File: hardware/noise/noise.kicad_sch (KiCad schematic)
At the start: 66 parts, among them J1 Conn_02x05_Odd_Even, J2 White, J3 Pink, J4 Blue, J5 Grainy, J6 HP Grainy, Q1 BC547, U1 TL074, U2 TL072

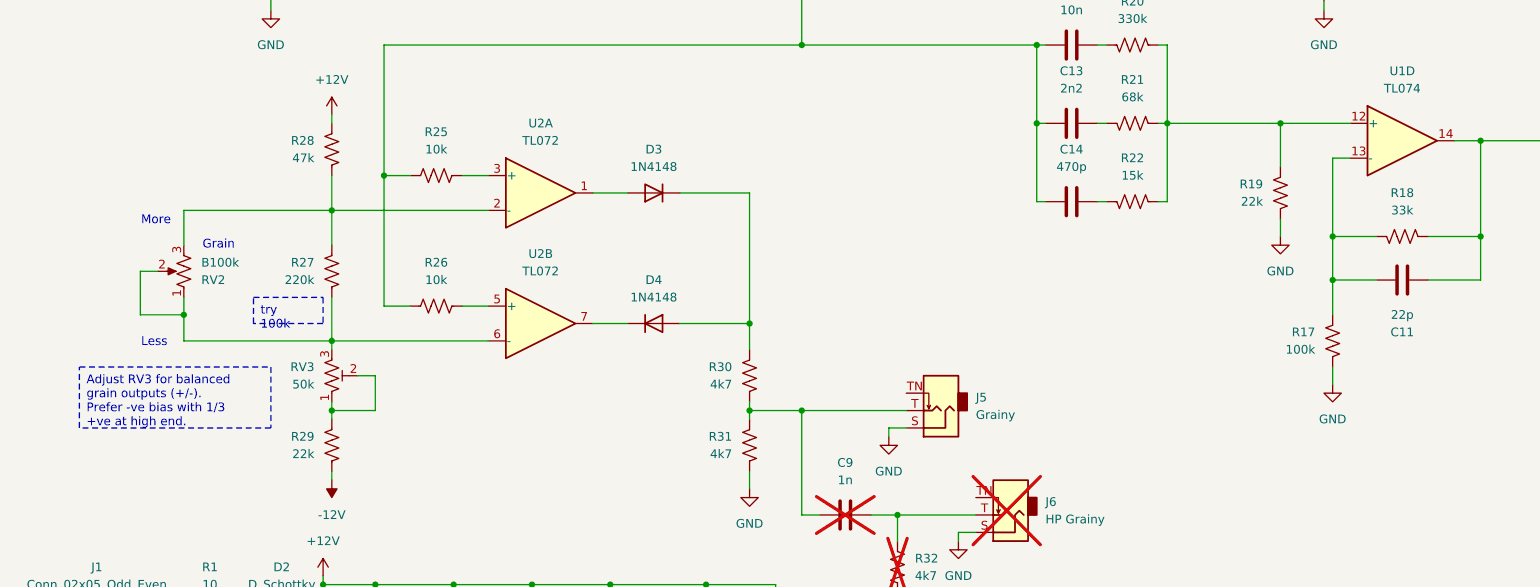
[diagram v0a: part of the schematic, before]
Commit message: finished design checks on grain output and update schematic/layout to v1.1
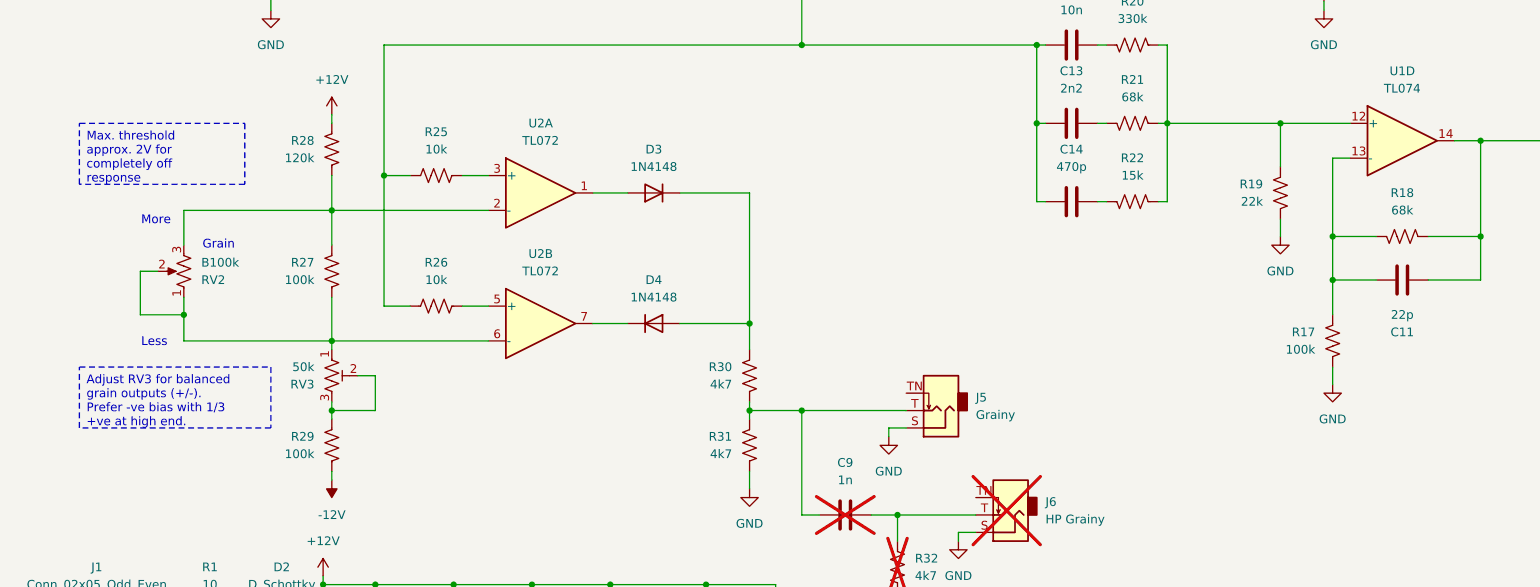
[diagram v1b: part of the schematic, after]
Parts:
- C12, C6: footprint Capacitor_THT:C_Rect_L13.0mm_W4.0mm_P10.00mm_FKS3_FKP3_MKS4 -> Capacitor_THT:C_Rect_L7.0mm_W3.5mm_P5.00mm
- C14, C8: footprint Capacitor_THT:C_Rect_L7.0mm_W3.5mm_P5.00mm -> Capacitor_THT:C_Disc_D4.7mm_W2.5mm_P5.00mm
- J2, J3, J4, J5, J6: footprint AudioJacks:Jack_3.5mm_QingPu_WQP-PJ316M_Horizontal_1 -> AudioJacks:Jack_3.5mm_QingPu_WQP-PJ323M_Horizontal
- R18: value 33k -> 68k
- R27: value 220k -> 100k
- R28: value 47k -> 120k
- R29: value 22k -> 100k
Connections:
- net at R27.2, RV2.1, RV2.2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: now also RV3.1; no longer RV3.3
- net at R29.1, RV3.2: now also RV3.3; no longer RV3.1
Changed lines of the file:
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@@
 	(title_block
 		(title "Random Noise")
-		(date "2025-02-07")
-		(rev "1.0")
+		(date "2025-03-08")
+		(rev "1.1")
 		(company "idyllm")
 		(comment 1 "CC BY-SA 4.0")
@@
 		)
 	)
-	(text_box "Adjust RV3 for balanced grain outputs (+/-).\nPrefer -ve bias with 1/3 +ve at high end."
+	(text_box "Max. threshold approx. 2V for completely off response"
 		(exclude_from_sim no)
-		(at 33.02 139.7 0)
-		(size 27.94 8.89)
+		(at 33.02 104.14 0)
+		(size 24.13 8.89)
 		(stroke
 			(width 0)
@@
 		)
 	)
-	(text_box "try 100k"
+	(text_box "Adjust RV3 for balanced grain outputs (+/-).\nPrefer -ve bias with 1/3 +ve at high end."
 		(exclude_from_sim no)
-		(at 58.42 129.54 0)
-		(size 10.16 3.81)
+		(at 33.02 139.7 0)
+		(size 27.94 8.89)
 		(stroke
 			(width 0)
@@
 			)
 		)
-		(property "Footprint" "AudioJacks:Jack_3.5mm_QingPu_WQP-PJ316M_Horizontal_1"
+		(property "Footprint" "AudioJacks:Jack_3.5mm_QingPu_WQP-PJ323M_Horizontal"
 			(at 168.91 161.29 0)
 			(effects
@@
 			)
 		)
-		(property "Value" "47k"
+		(property "Value" "120k"
 			(at 67.31 109.2199 0)
 			(effects
@@
 			)
 		)
-		(property "Value" "220k"
+		(property "Value" "100k"
 			(at 67.31 126.9999 0)
 			(effects
@@
 		(lib_id "Device:R_Potentiometer_Trim_US")
 		(at 69.85 140.97 0)
-		(mirror x)
 		(unit 1)
 		(exclude_from_sim no)
@@
 		(on_board yes)
 		(dnp no)
-		(fields_autoplaced yes)
 		(property "Reference" "RV3"
-			(at 67.31 139.6999 0)
+			(at 67.31 142.2401 0)
 			(effects
 				(font
@@
 		)
 		(property "Value" "50k"
-			(at 67.31 142.2399 0)
+			(at 67.31 139.7001 0)
 			(effects
 				(font
@@
 			)
 		)
-		(property "Footprint" "AudioJacks:Jack_3.5mm_QingPu_WQP-PJ316M_Horizontal_1"
+		(property "Footprint" "AudioJacks:Jack_3.5mm_QingPu_WQP-PJ323M_Horizontal"
 			(at 267.97 57.15 0)
 			(effects
@@
 			)
 		)
-		(property "Footprint" "Capacitor_THT:C_Rect_L7.0mm_W3.5mm_P5.00mm"
+		(property "Footprint" "Capacitor_THT:C_Disc_D4.7mm_W2.5mm_P5.00mm"
 			(at 173.99 114.6048 0)
 			(effects
@@
 			)
 		)
-		(property "Footprint" "Capacitor_THT:C_Rect_L7.0mm_W3.5mm_P5.00mm"
+		(property "Footprint" "Capacitor_THT:C_Disc_D4.7mm_W2.5mm_P5.00mm"
 			(at 179.3748 55.88 0)
 			(effects
@@
 			)
 		)
-		(property "Footprint" "Capacitor_THT:C_Rect_L13.0mm_W4.0mm_P10.00mm_FKS3_FKP3_MKS4"
+		(property "Footprint" "Capacitor_THT:C_Rect_L7.0mm_W3.5mm_P5.00mm"
 			(at 173.99 91.7448 0)
 			(effects
@@
 			)
 		)
-		(property "Footprint" "AudioJacks:Jack_3.5mm_QingPu_WQP-PJ316M_Horizontal_1"
+		(property "Footprint" "AudioJacks:Jack_3.5mm_QingPu_WQP-PJ323M_Horizontal"
 			(at 267.97 106.68 0)
 			(effects
@@
 			)
 		)
-		(property "Footprint" "AudioJacks:Jack_3.5mm_QingPu_WQP-PJ316M_Horizontal_1"
+		(property "Footprint" "AudioJacks:Jack_3.5mm_QingPu_WQP-PJ323M_Horizontal"
 			(at 158.75 146.05 0)
 			(effects
@@
 			)
 		)
-		(property "Footprint" "Capacitor_THT:C_Rect_L13.0mm_W4.0mm_P10.00mm_FKS3_FKP3_MKS4"
+		(property "Footprint" "Capacitor_THT:C_Rect_L7.0mm_W3.5mm_P5.00mm"
 			(at 156.5148 55.88 0)
 			(effects
@@
 			)
 		)
-		(property "Value" "22k"
+		(property "Value" "100k"
 			(at 67.31 152.3999 0)
 			(effects
@@
 			)
 		)
-		(property "Footprint" "AudioJacks:Jack_3.5mm_QingPu_WQP-PJ316M_Horizontal_1"
+		(property "Footprint" "AudioJacks:Jack_3.5mm_QingPu_WQP-PJ323M_Horizontal"
 			(at 267.97 27.94 0)
 			(effects
@@
 			)
 		)
-		(property "Value" "33k"
+		(property "Value" "68k"
 			(at 226.06 116.84 90)
 			(effects

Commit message: Submitted board v1.1 for fab
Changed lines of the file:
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@@
 	(title_block
 		(title "Random Noise")
-		(date "2025-03-08")
+		(date "2025-03-09")
 		(rev "1.1")
 		(company "idyllm")
@@
 	(wire
 		(pts
-			(xy 36.83 22.86) (xy 36.83 36.83)
+			(xy 36.83 31.75) (xy 36.83 36.83)
 		)
 		(stroke
@@
 		)
 	)
-	(text_box "Increasing R6 to 150k increases bias to negative Vpk and reduces amplitude"
-		(exclude_from_sim no)
-		(at 40.64 29.21 0)
-		(size 29.21 7.62)
-		(stroke
-			(width 0)
-			(type dash)
-		)
-		(fill
-			(type none)
-		)
-		(effects
-			(font
-				(size 1.27 1.27)
-			)
-			(justify left top)
-		)
-	)
 	(text "Grain"
 		(exclude_from_sim no)
@@
 	(symbol
 		(lib_id "power:+12V")
-		(at 36.83 22.86 0)
+		(at 36.83 31.75 0)
 		(unit 1)
 		(exclude_from_sim no)
@@
 		(fields_autoplaced yes)
 		(property "Reference" "#PWR08"
-			(at 36.83 26.67 0)
+			(at 36.83 35.56 0)
 			(effects
 				(font
@@
 		)
 		(property "Value" "+12V"
-			(at 36.83 17.78 0)
+			(at 36.83 26.67 0)
 			(effects
 				(font
@@
 		)
 		(property "Footprint" ""
-			(at 36.83 22.86 0)
+			(at 36.83 31.75 0)
 			(effects
 				(font
@@
 		)
 		(property "Datasheet" ""
-			(at 36.83 22.86 0)
+			(at 36.83 31.75 0)
 			(effects
 				(font
@@
 		)
 		(property "Description" "Power symbol creates a global label with name \"+12V\""
-			(at 36.83 22.86 0)
+			(at 36.83 31.75 0)
 			(effects
 				(font

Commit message: Fixed bad orientation for IDC header to support horizontal and vertical plugs
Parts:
- J1: footprint Connector_IDC:IDC-Header_2x05_P2.54mm_Vertical -> Connector_IDC:IDC-Header_2x05_P2.54mm_Horizontal
- R2: footprint Resistor_THT:R_Axial_DIN0207_L6.3mm_D2.5mm_P10.16mm_Horizontal -> Resistor_THT:R_Axial_DIN0207_L6.3mm_D2.5mm_P2.54mm_Vertical
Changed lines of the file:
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@@
 	(title_block
 		(title "Random Noise")
-		(date "2025-03-09")
-		(rev "1.1")
+		(date "2025-03-12")
+		(rev "1.2")
 		(company "idyllm")
 		(comment 1 "CC BY-SA 4.0")
@@
 			)
 		)
-		(property "Footprint" "Resistor_THT:R_Axial_DIN0207_L6.3mm_D2.5mm_P10.16mm_Horizontal"
+		(property "Footprint" "Resistor_THT:R_Axial_DIN0207_L6.3mm_D2.5mm_P2.54mm_Vertical"
 			(at 52.324 184.404 90)
 			(effects
@@
 			)
 		)
-		(property "Footprint" "Connector_IDC:IDC-Header_2x05_P2.54mm_Vertical"
+		(property "Footprint" "Connector_IDC:IDC-Header_2x05_P2.54mm_Horizontal"
 			(at 34.29 180.34 0)
 			(effects
